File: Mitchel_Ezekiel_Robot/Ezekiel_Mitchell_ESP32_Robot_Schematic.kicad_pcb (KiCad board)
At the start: 2 copper layers, 138.9 x 83.3 mm, 33 parts, among them J1 JTAG, J2 GPS MODULE, J3 Barrel_Jack_Switch, J4 Conn_01x06, J5 Conn_01x06, J6 Conn_01x04, J7 Conn_02x03_Odd_Even, Q1 SFH300, SW1 SW_SPST, U1 ESP32-DEVKITC-32E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

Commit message: pcb edit
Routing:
- net +BATT: track 203.1 -> 0.00 mm
- net /TRIG: track 132.9 -> 0.00 mm
- net /RENCODER_B: track 123.0 -> 0.00 mm
- net /ECHO: track 115.4 -> 0.00 mm
- net /HORN: track 71.1 -> 0.00 mm
- net GND: track 23.3 -> 0.00 mm

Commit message: update pcb edit
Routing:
- net +BATT: track 0.00 -> 511.8 mm
- net /RENCODER_B: track 0.00 -> 172.9 mm, vias 0 -> 1
- net /ECHO: track 0.00 -> 131.0 mm
- net /TRIG: track 0.00 -> 112.7 mm
- net /HORN: track 0.00 -> 39.6 mm
- net GND: track 0.00 -> 7.16 mm
- net /REARLAMPS: track 119.5 -> 121.9 mm
- net +3V3: track 244.9 -> 247.0 mm
- net /RPWM_1A2A: track 192.7 -> 194.0 mm
- net /RMOTOR_1A: track 69.5 -> 68.3 mm
- net /PHOTOTRANS: track 120.4 -> 121.2 mm
- net /JTAG_MTDI: track 31.0 -> 30.3 mm
- net /JTAG_MTDO: track 59.0 -> 58.3 mm
- net /JTAG_MTCK: track 19.1 -> 18.4 mm

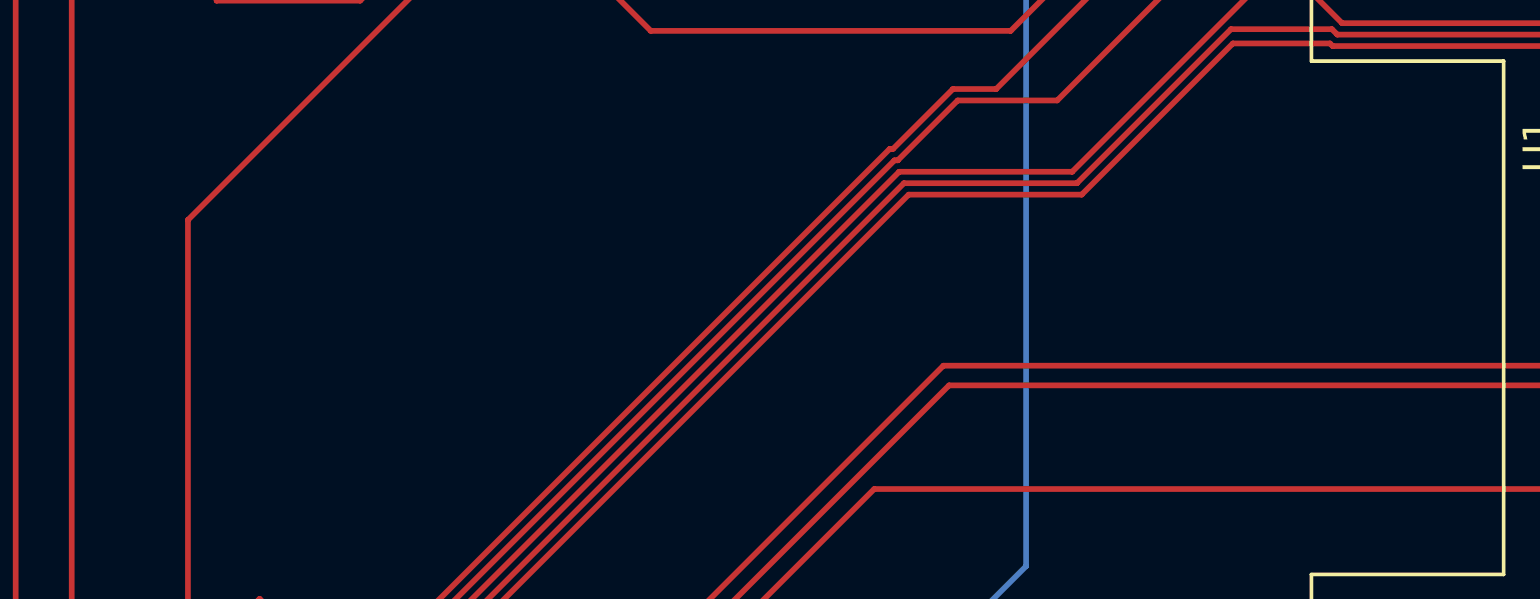
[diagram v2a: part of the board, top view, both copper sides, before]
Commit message: caster insert
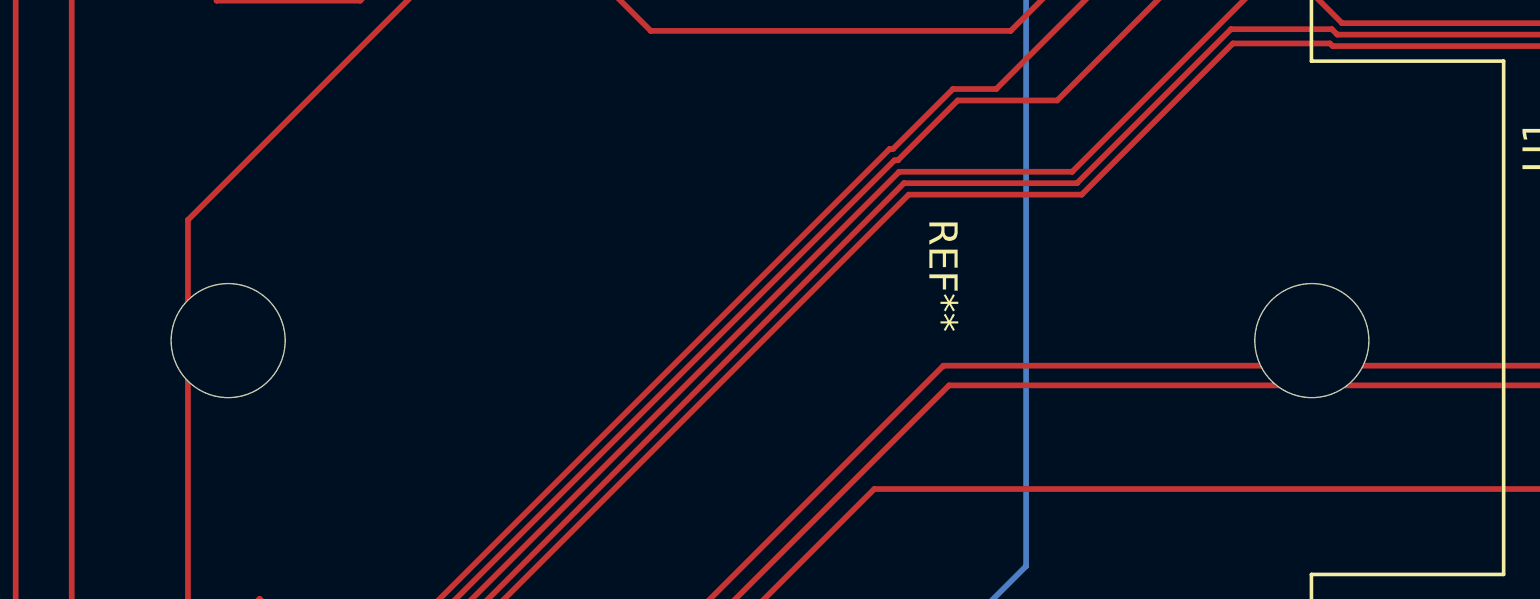
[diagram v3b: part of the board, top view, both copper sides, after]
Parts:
- added REF**: Ball-Caster-1, 0-My-Library:Ball-Caster-1, F.Cu at (120.2, 89.9)
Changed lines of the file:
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@@
 		)
+	)
+	(footprint "0-My-Library:Ball-Caster-1"
+		(layer "F.Cu")
+		(at 120.22 89.92 -90)
+		(property "Reference" "REF**"
+			(at -2.286 12.954 270)
+			(unlocked yes)
+			(layer "F.SilkS")
+			(effects
+				(font
+					(size 1 1)
+					(thickness 0.1)
+				)
+			)
+		)
+		(property "Value" "Ball-Caster-1"
+			(at -0.254 11.176 270)
+			(unlocked yes)
+			(layer "F.Fab")
+			(effects
+				(font
+					(size 1 1)
+					(thickness 0.15)
+				)
+			)
+		)
+		(property "Datasheet" ""
+			(at 0 0 270)
+			(unlocked yes)
+			(layer "F.Fab")
+			(hide yes)
+			(effects
+				(font
+					(size 1 1)
+					(thickness 0.15)
+				)
+			)
+		)
+		(property "Description" ""
+			(at 0 0 270)
+			(unlocked yes)
+			(layer "F.Fab")
+			(hide yes)
+			(effects
+				(font
+					(size 1 1)
+					(thickness 0.15)
+				)
+			)
+		)
+		(attr through_hole)
+		(fp_circle
+			(center 0 38)
+			(end 4 38)
+			(stroke
+				(width 0.15)
+				(type solid)
+			)
+			(fill no)
+			(layer "Cmts.User")
+		)
+		(fp_circle
+			(center 0 0)
+			(end 4 0)
+			(stroke
+				(width 0.15)
+				(type solid)
+			)
+			(fill no)
+			(layer "Cmts.User")
+		)
+		(fp_circle
+			(center 0 38)
+			(end 4.25 38)
+			(stroke
+				(width 0.05)
+				(type solid)
+			)
+			(fill no)
+			(layer "F.CrtYd")
+		)
+		(fp_circle
+			(center 0 0)
+			(end 4.25 0)
+			(stroke
+				(width 0.05)
+				(type solid)
+			)
+			(fill no)
+			(layer "F.CrtYd")
+		)
+		(pad "" np_thru_hole circle
+			(at 0 0 270)
+			(size 4 4)
+			(drill 4)
+			(layers "*.Cu" "*.Mask")
+		)
+		(pad "" np_thru_hole circle
+			(at 0 38 270)
+			(size 4 4)
+			(drill 4)
+			(layers "*.Cu" "*.Mask")
+		)
+		(embedded_fonts no)
 	)
 	(footprint "Button_Switch_THT:SW_CW_GPTS203211B"
